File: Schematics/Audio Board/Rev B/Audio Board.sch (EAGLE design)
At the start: 26 parts, among them IC1 7803, IC2 7810-LDO, IC3 STM32F303CBT7, IC4 AK4430ET, IC5 PCA9600SO8, J1 503398-1892, J2 LINEOUT_R, J3 LINEOUT_L, J4 54602-908LF, J5 54602-908LF, J6 54602-908LF, X2 22-23-2031

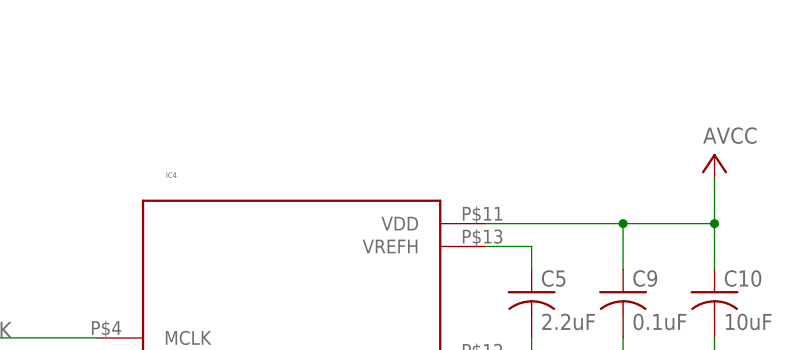
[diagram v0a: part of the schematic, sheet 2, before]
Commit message: Small changes to Audio Board Rev B and add Gerbers
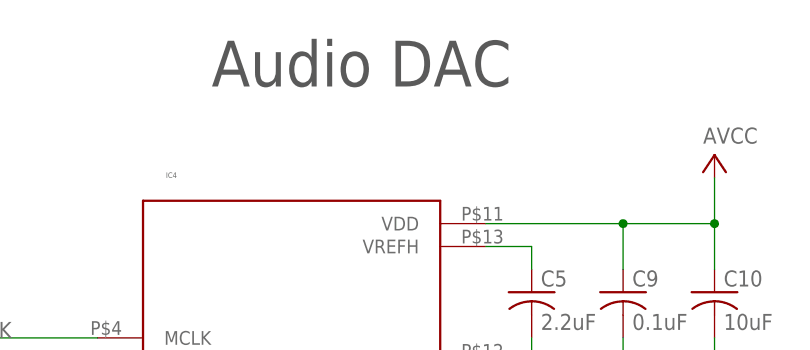
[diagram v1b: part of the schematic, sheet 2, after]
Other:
- note added: "Audio DAC"
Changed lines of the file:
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@@
 <class number="0" name="default" width="0" drill="0">
 </class>
-<class number="1" name="power" width="0.3048" drill="0.3048">
+<class number="1" name="power" width="0.3048" drill="0">
 <clearance class="0" value="0.1524"/>
 <clearance class="1" value="0.1524"/>
@@
 <sheet>
 <plain>
+<text x="109.22" y="147.32" size="5.08" layer="97">Audio DAC</text>
 </plain>
 <instances>

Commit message: Minor revisions to Audio Board Rev B
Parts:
- renumbered X2 to SERIAL
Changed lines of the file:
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@@
 <part name="C2" library="rcl" library_urn="urn:adsk.eagle:library:334" deviceset="C-US" device="025-025X050" package3d_urn="urn:adsk.eagle:package:23629/2" value="1uF"/>
 <part name="J1" library="503398-1892" deviceset="503398-1892" device=""/>
-<part name="X2" library="con-molex" library_urn="urn:adsk.eagle:library:165" deviceset="22-23-2031" device="" package3d_urn="urn:adsk.eagle:package:8078634/1"/>
+<part name="SERIAL" library="con-molex" library_urn="urn:adsk.eagle:library:165" deviceset="22-23-2031" device="" package3d_urn="urn:adsk.eagle:package:8078634/1"/>
 <part name="GND4" library="supply1" library_urn="urn:adsk.eagle:library:371" deviceset="GND" device=""/>
 <part name="FRAME2" library="frames" library_urn="urn:adsk.eagle:library:229" deviceset="LETTER_L" device=""/>
@@
 <attribute name="VALUE" x="241.304" y="152.4056" size="1.778559375" layer="96" rot="MR0"/>
 </instance>
-<instance part="X2" gate="-1" x="182.88" y="147.32" smashed="yes">
+<instance part="SERIAL" gate="-1" x="182.88" y="147.32" smashed="yes">
 <attribute name="NAME" x="185.42" y="146.558" size="1.524" layer="95"/>
 </instance>
-<instance part="X2" gate="-2" x="182.88" y="149.86" smashed="yes">
+<instance part="SERIAL" gate="-2" x="182.88" y="149.86" smashed="yes">
 <attribute name="NAME" x="185.42" y="149.098" size="1.524" layer="95"/>
 </instance>
-<instance part="X2" gate="-3" x="182.88" y="152.4" smashed="yes">
+<instance part="SERIAL" gate="-3" x="182.88" y="152.4" smashed="yes">
 <attribute name="NAME" x="185.42" y="151.638" size="1.524" layer="95"/>
 </instance>
@@
 </segment>
 <segment>
-<pinref part="X2" gate="-3" pin="S"/>
+<pinref part="SERIAL" gate="-3" pin="S"/>
 <pinref part="GND4" gate="1" pin="GND"/>
 <wire x1="180.34" y1="154.94" x2="180.34" y2="152.4" width="0.1524" layer="91"/>
@@
 <net name="RX" class="0">
 <segment>
-<pinref part="X2" gate="-2" pin="S"/>
+<pinref part="SERIAL" gate="-2" pin="S"/>
 <wire x1="175.26" y1="149.86" x2="180.34" y2="149.86" width="0.1524" layer="91"/>
 <label x="167.64" y="149.86" size="1.778" layer="95"/>
@@
 <net name="TX" class="0">
 <segment>
-<pinref part="X2" gate="-1" pin="S"/>
+<pinref part="SERIAL" gate="-1" pin="S"/>
 <wire x1="180.34" y1="147.32" x2="165.1" y2="147.32" width="0.1524" layer="91"/>
 <pinref part="IC3" gate="G$1" pin="PA9/I2C2_SCL"/>
